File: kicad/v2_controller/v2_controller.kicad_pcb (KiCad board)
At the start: 4 copper layers, 100 x 116 mm, 134 parts, among them J1 USB_C_Receptacle_USB2.0, J2 USB_C_Receptacle_USB2.0, J3 Conn_02x10_Odd_Even, J4 Conn_02x10_Odd_Even, J5 Conn_02x04_Odd_Even, J6 Conn_02x03_Odd_Even, Q1 S8050, Q2 S8050, SW1 KP0, SW10 KP7, SW11 KP8, SW12 KP9, SW13 KP_Plus, SW14 KP_Extra, SW15 KP_Divide, SW16 KP_Multiply, SW17 KP_Subtract, SW18 Boot, SW19 Reset, SW2 KP_Dot, SW3 KP1, SW4 KP2, SW5 KP3, SW6 KP_Enter, SW7 KP4, SW8 KP5, SW9 KP6, U1 ESP32-S3-WROOM-1-N16R8, U2 SSD1306_I2C, U3 74AHCT1G125, U4 NCP167BMX330TBG, U5 USBLC6-2SC6, U6 USBLC6-2P6, U7 CP2102N-Axx-xQFN24

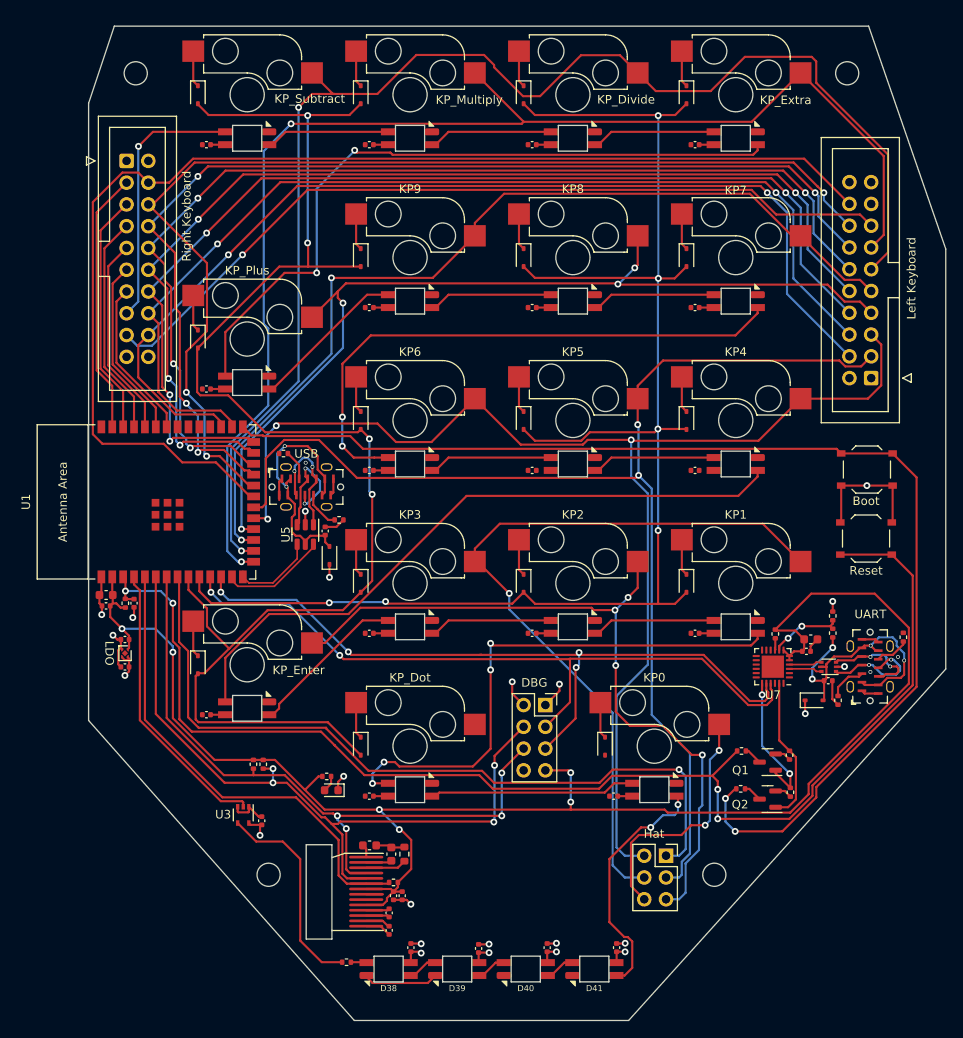
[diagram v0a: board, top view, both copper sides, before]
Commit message: [kicad] fix key locations
The key locations were previously off by 1mm in the Y axis.
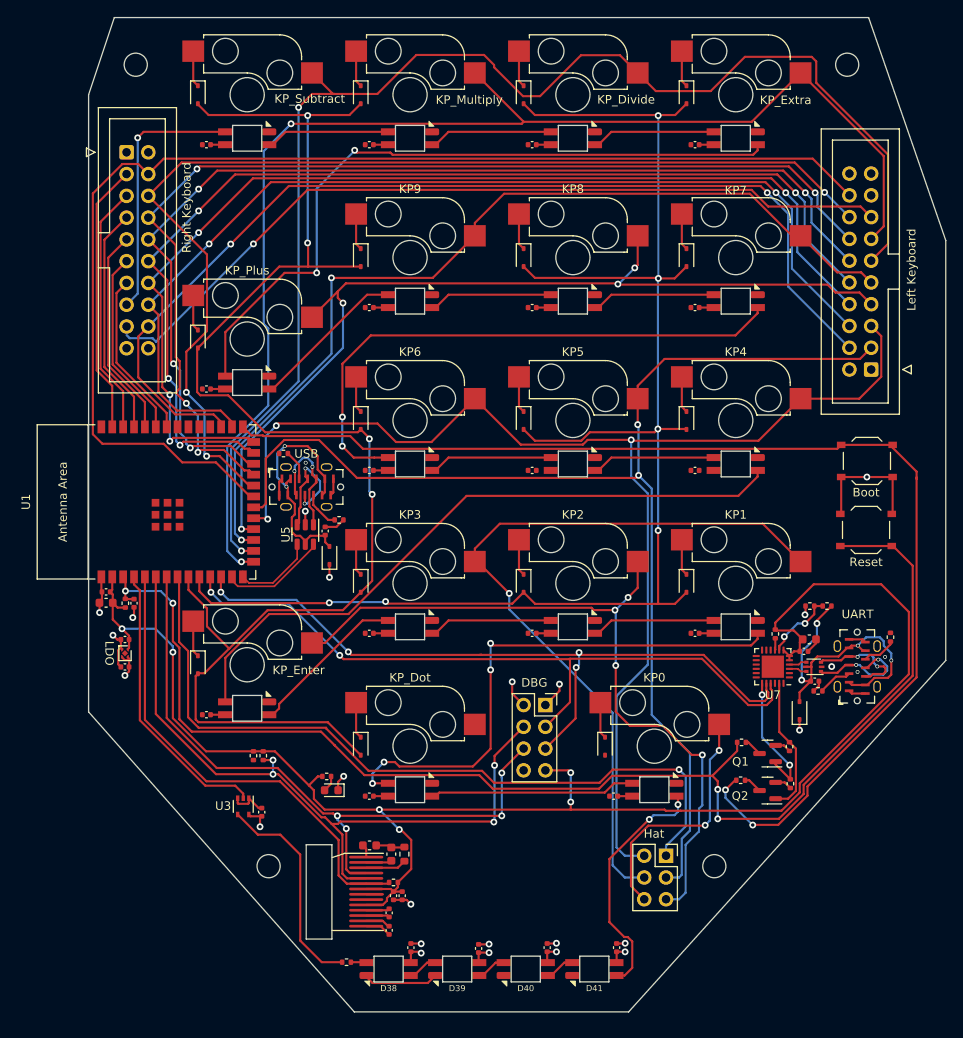
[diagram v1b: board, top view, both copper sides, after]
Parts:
- moved R13 3.22 mm to (129.2, 107.7), turned to 180 degrees
- moved R14 2.90 mm to (127.2, 107.7), turned to 180 degrees
- moved R10 2.57 mm to (128.1, 117.6), turned to 180 degrees
- moved D19 2.07 mm to (125.9, 119.8), turned to 90 degrees
- moved U6 1.76 mm to (127.6, 114.7)
- moved C3 1.63 mm to (45.0, 106.0)
- moved C16 1.57 mm to (127.7, 116.4)
- moved J2 1.50 mm to (132.7, 114.7)
- moved R11 1.50 mm to (136.5, 111.3)
- moved C10 1.00 mm to (63.2, 131.7)
- moved J3 1.00 mm to (134.3, 80.1)
- moved J4 1.00 mm to (47.4, 54.7)
- moved MH1 1.00 mm to (48.5, 44.5)
- moved MH2 1.00 mm to (131.5, 44.5)
- moved MH3 1.00 mm to (64.0, 138.0)
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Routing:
- net /USB/UART_USB_VBUS: track 33.0 -> 37.8 mm
- net GND: track 75.9 -> 73.0 mm
- net /USB/UART_USB_D-: track 3.85 -> 2.10 mm
- net /USB/UART_USB_D+: track 3.86 -> 2.11 mm
- net /ESP32/CHIP_PU: track 151.4 -> 152.7 mm
- net +3.3V: track 188.2 -> 189.3 mm
- net /ESP32/UART_RTS: track 16.3 -> 15.3 mm
- net /ESP32/UART_DTR: track 17.1 -> 16.1 mm
- net /ESP32/ROW9: track 23.5 -> 24.5 mm
- net /ESP32/ROW8: track 55.8 -> 56.8 mm
- net /ESP32/ROW6: track 119.8 -> 120.8 mm
- net /ESP32/ROW10: track 21.1 -> 22.1 mm
- net /ESP32/ROW1: track 159.7 -> 158.7 mm
- net /ESP32/ROW0: track 151.9 -> 150.9 mm
- net /ESP32/ROW11: track 18.7 -> 19.7 mm
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
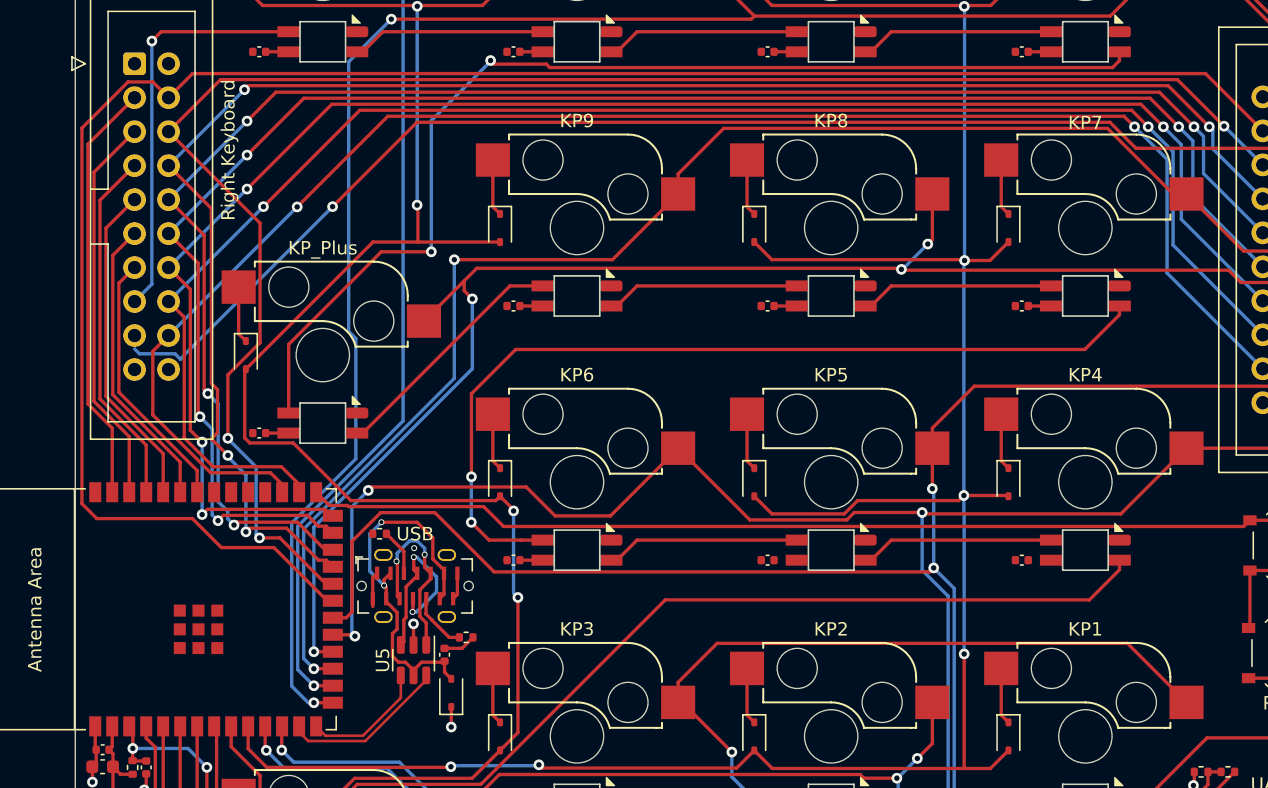
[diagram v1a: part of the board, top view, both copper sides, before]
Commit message: [kicad] finish connecting remaining rows
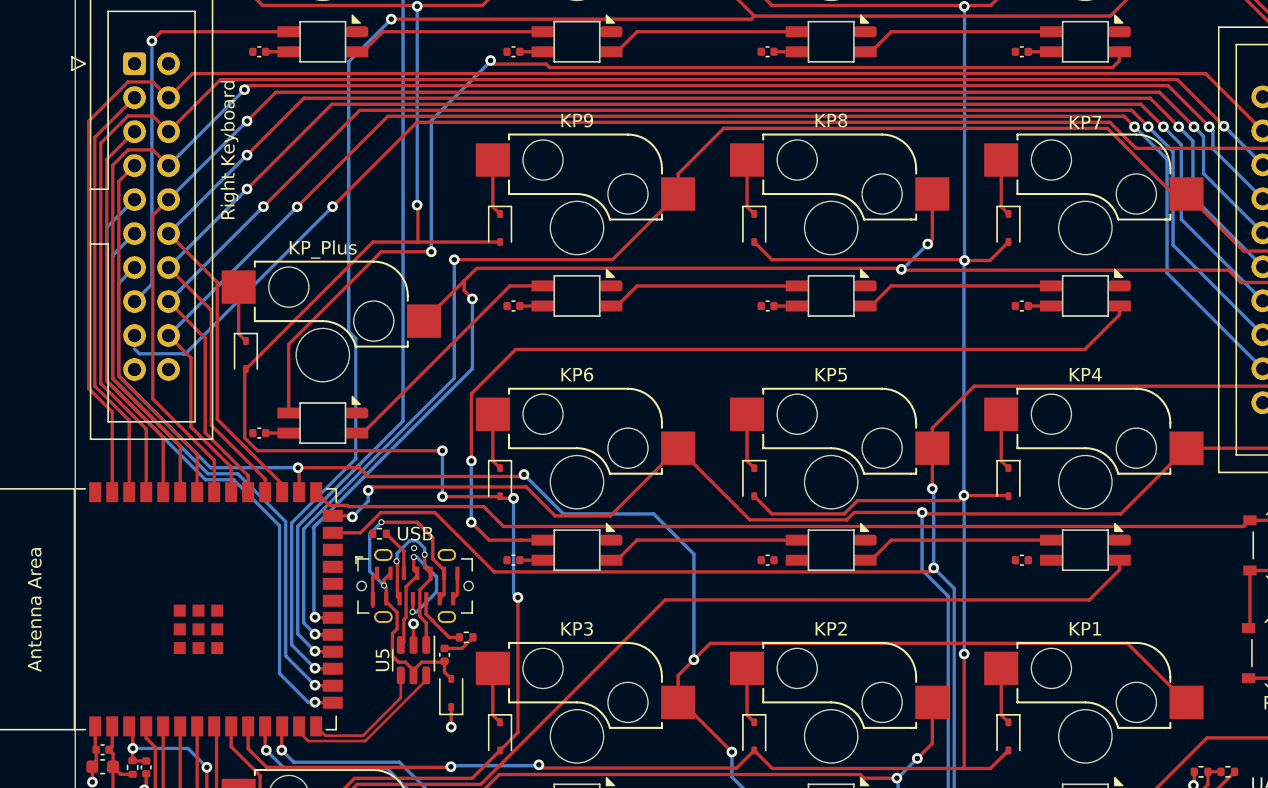
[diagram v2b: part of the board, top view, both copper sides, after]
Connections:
- J4 pad 11: /ESP32/ROW10 -> /ESP32/ROW7
- J4 pad 13: /ESP32/ROW11 -> /ESP32/ROW6
- J4 pad 3: /ESP32/ROW6 -> /ESP32/ROW11
- J4 pad 5: /ESP32/ROW7 -> /ESP32/ROW10
- J4 pad 7: /ESP32/ROW8 -> /ESP32/ROW9
- J4 pad 9: /ESP32/ROW9 -> /ESP32/ROW8
- U1 pad 15: /ESP32/ROW0 -> /ESP32/ROW8
- U1 pad 16: /ESP32/ROW1 -> /ESP32/ROW7
- U1 pad 17: /ESP32/ROW2 -> /ESP32/ROW0
- U1 pad 18: /ESP32/ROW3 -> /ESP32/ROW1
- U1 pad 19: /ESP32/ROW4 -> /ESP32/ROW2
- U1 pad 20: /ESP32/ROW5 -> /ESP32/ROW3
- U1 pad 21: /ESP32/COL0 -> unconnected-(U1-GPIO13-Pad21)
- U1 pad 22: /ESP32/COL1 -> unconnected-(U1-GPIO14-Pad22)
- U1 pad 23: /ESP32/COL2 -> unconnected-(U1-GPIO21-Pad23)
- U1 pad 24: /ESP32/COL3 -> unconnected-(U1-GPIO47/SPICLK_P-Pad24)
- U1 pad 25: /ESP32/COL4 -> /ESP32/ROW5
- U1 pad 26: /ESP32/COL5 -> /ESP32/ROW4
- U1 pad 28: /ESP32/COL6 -> /ESP32/ROW6
- U1 pad 29: /ESP32/COL7 -> /ESP32/COL4
- U1 pad 30: unconnected-(U1-GPIO37-Pad30) -> /ESP32/COL5
- U1 pad 31: unconnected-(U1-GPIO38-Pad31) -> /ESP32/COL6
- U1 pad 32: unconnected-(U1-GPIO39-Pad32) -> /ESP32/COL7
- U1 pad 33: unconnected-(U1-GPIO40-Pad33) -> /ESP32/COL3
- U1 pad 34: /ESP32/ROW11 -> /ESP32/ROW9
- U1 pad 35: /ESP32/ROW10 -> /ESP32/COL2
- U1 pad 36: /ESP32/ROW9 -> /ESP32/ROW10
- U1 pad 37: /ESP32/ROW8 -> /ESP32/COL1
- U1 pad 38: /ESP32/ROW7 -> /ESP32/ROW11
- U1 pad 39: /ESP32/ROW6 -> /ESP32/COL0
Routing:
- net /ESP32/ROW6: track 120.8 -> 156.4 mm, vias 1 -> 4
- net /ESP32/COL0: track 142.5 -> 120.4 mm
- net /ESP32/ROW8: track 56.8 -> 77.7 mm, vias 2 -> 3
- net /ESP32/ROW7: track 116.8 -> 130.9 mm, vias 4 -> 5
- net /ESP32/ROW11: track 19.7 -> 31.8 mm
- net /ESP32/COL3: track 125.8 -> 115.4 mm, vias 4 -> 2
- net /ESP32/COL5: track 125.8 -> 116.0 mm, vias 4 -> 2
- net /ESP32/COL4: track 126.0 -> 116.6 mm, vias 4 -> 2
- net /ESP32/ROW4: track 152.4 -> 143.1 mm
- net /ESP32/COL1: track 128.2 -> 119.9 mm, vias 3 -> 1
- net /ESP32/ROW10: track 22.1 -> 29.6 mm
- net /ESP32/COL2: track 126.7 -> 120.2 mm, vias 4 -> 2
- net /ESP32/ROW5: track 144.2 -> 138.5 mm
- net /ESP32/COL7: track 120.2 -> 115.0 mm
- net /ESP32/COL6: track 120.1 -> 115.5 mm
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
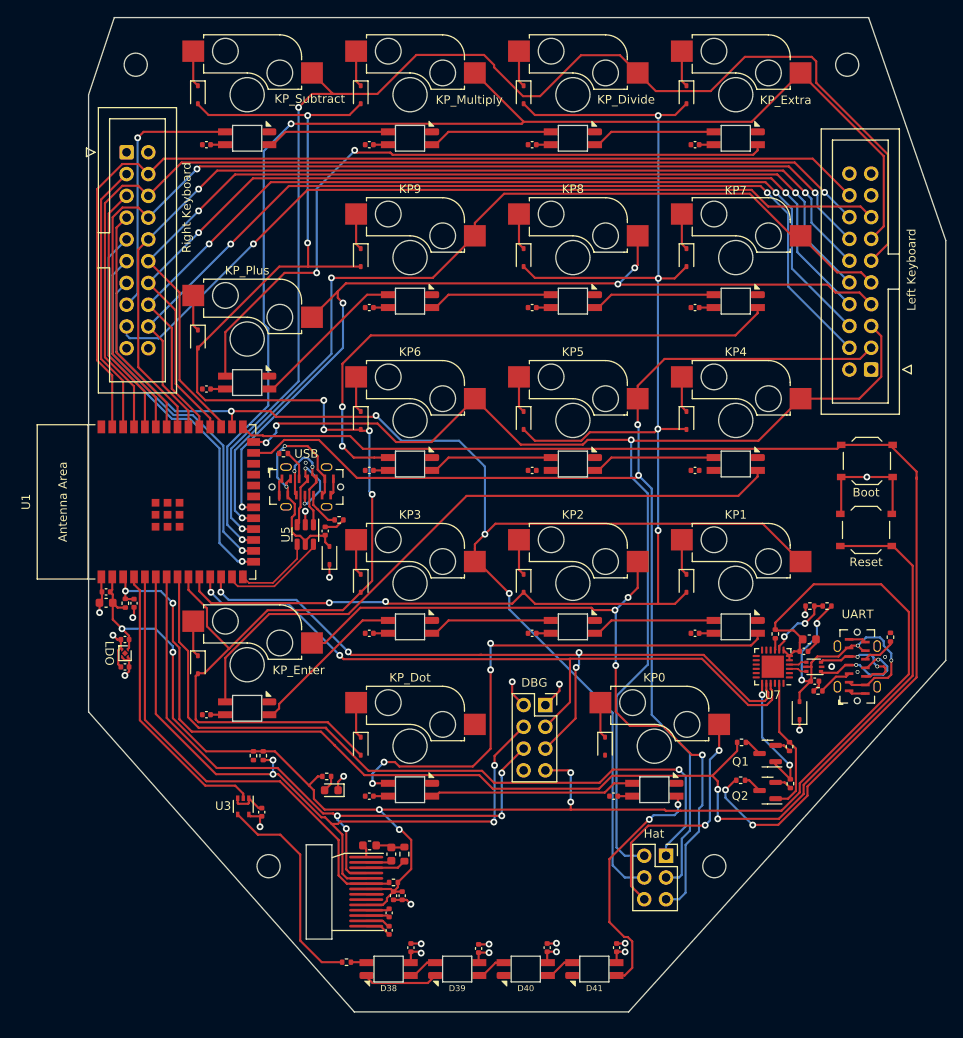
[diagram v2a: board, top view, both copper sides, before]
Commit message: [kicad] add ground and power planes, and finish connections
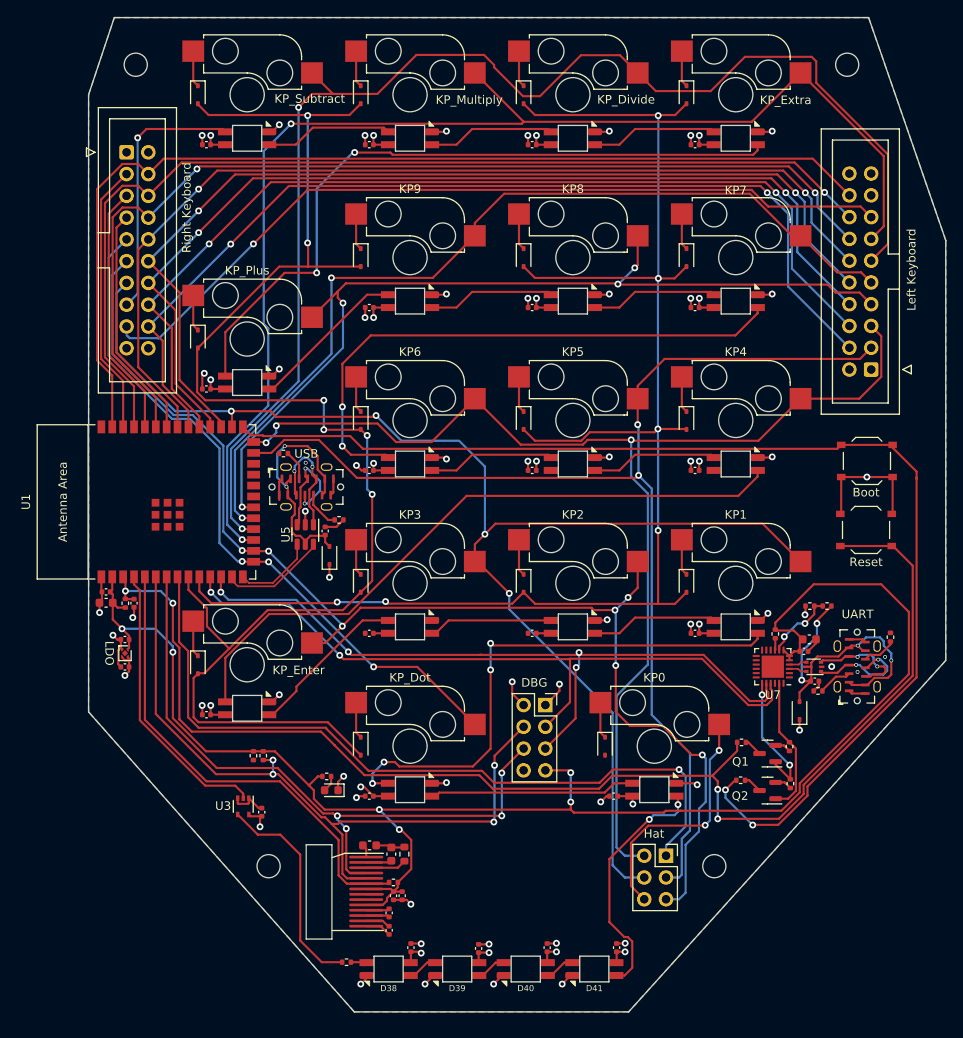
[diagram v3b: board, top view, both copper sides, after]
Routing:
- net GND: track 73.0 -> 115.4 mm, vias 17 -> 52
- net /ESP32/ROW8: track 77.7 -> 111.4 mm, vias 3 -> 5
- net +5V: track 48.0 -> 65.0 mm, vias 9 -> 24
- net /ESP32/ROW7: track 130.9 -> 145.3 mm, vias 5 -> 7
- added copper zone on In2.Cu, net +5V
- added copper zone on B.Cu, net GND
- added copper zone on F.Cu, net GND
- added copper zone on In1.Cu, net GND

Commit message: [kicad] clean up most PCB DRC violation issues
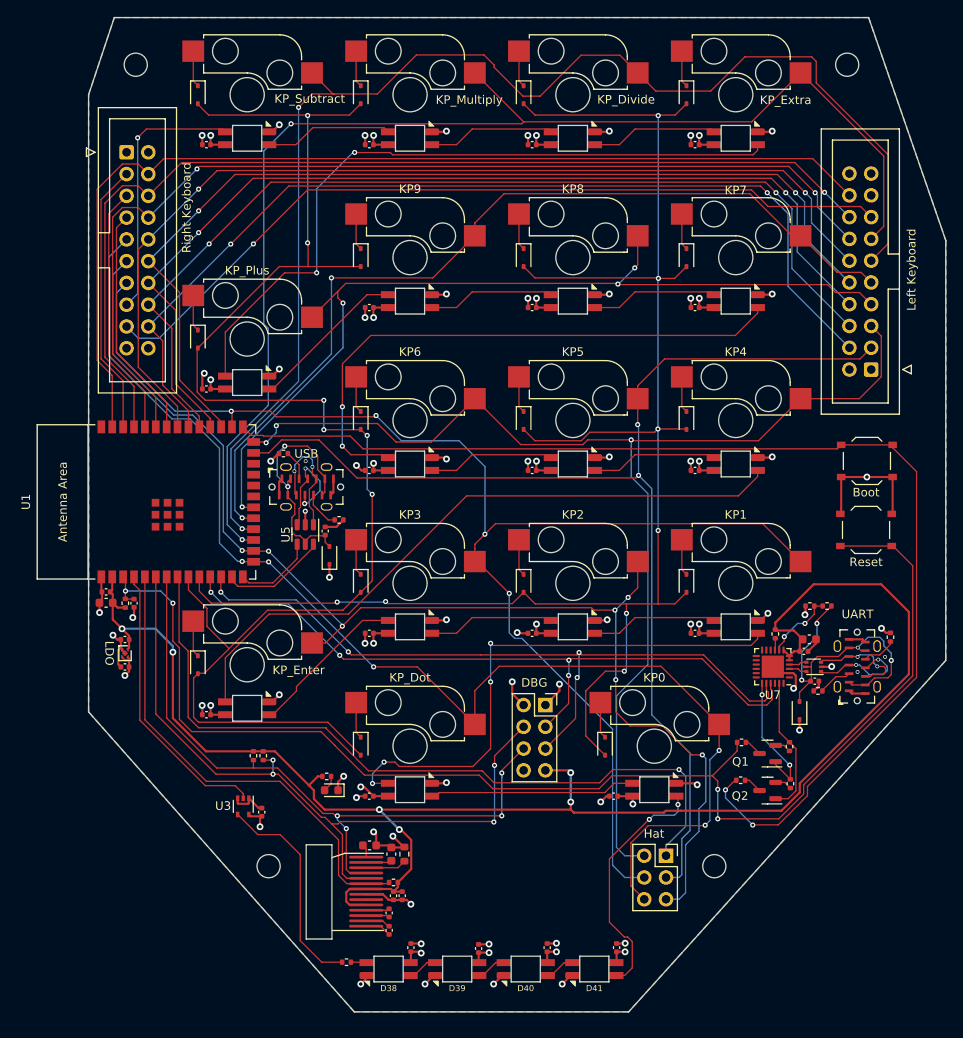
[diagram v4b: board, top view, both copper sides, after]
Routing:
- net /ESP32/ROW8: track 111.4 -> 147.8 mm
- net /ESP32/COL8: track 178.5 -> 200.2 mm, vias 6 -> 8
- net GND: track 115.4 -> 133.2 mm, vias 52 -> 60
- net +5V: track 65.0 -> 70.7 mm, vias 24 -> 26
- net +3.3V: track 189.4 -> 191.5 mm
- net /ESP32/SDA: track 78.6 -> 79.6 mm
- net /ESP32/UART_RX: track 84.2 -> 84.0 mm, vias 2 -> 4

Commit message: [kicad] address some additional constraints violations
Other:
- board text added: "JLCJLCJLCJLC"

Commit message: [kicad] clean up additional PCB issues
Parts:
- MH1, MH2, MH3, MH4: value MountingHole_2.7mm_M2.5 -> MountingHole_2.7mm_M2.5_Pad_Via; footprint MountingHole:MountingHole_2.7mm_M2.5 -> MountingHole:MountingHole_2.7mm_M2.5_Pad_Via
- U5: value USBLC6-2SC6 -> USBLC6-2P6; footprint Package_TO_SOT_SMD:SOT-23-6 -> Package_TO_SOT_SMD:SOT-666
